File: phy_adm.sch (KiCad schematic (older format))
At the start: 28 parts, among them U7 88E1545, U8 DSC1122CE1-125

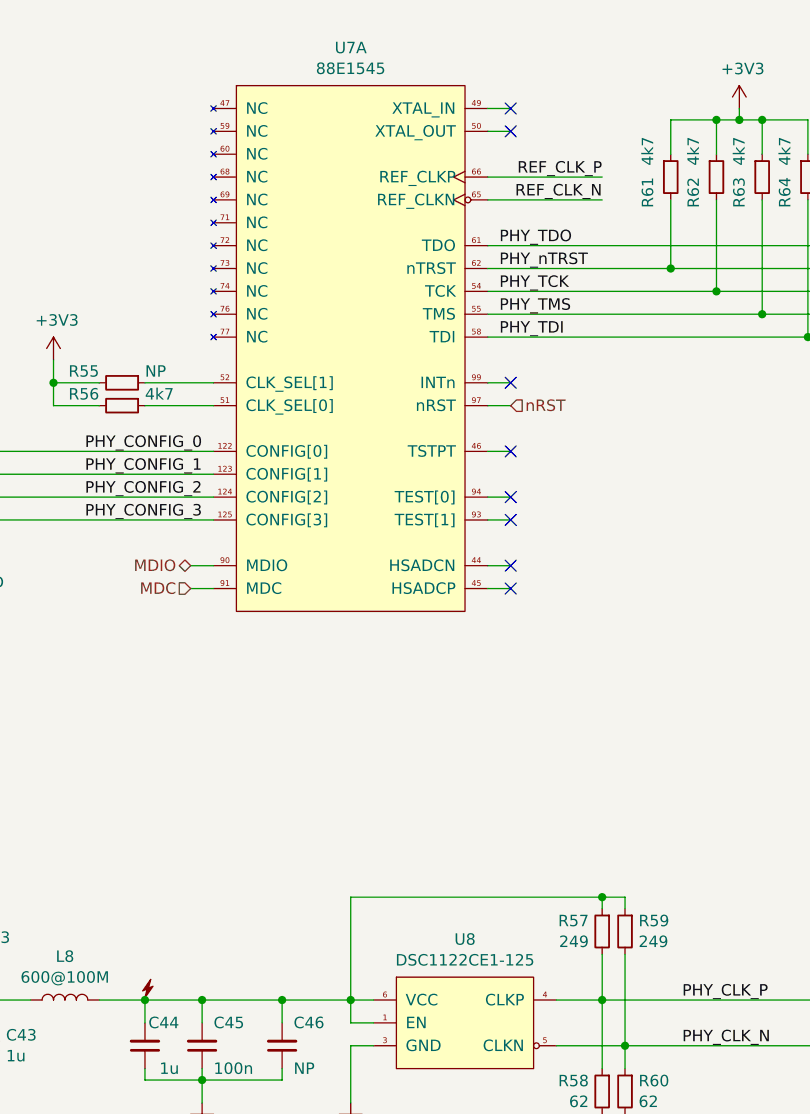
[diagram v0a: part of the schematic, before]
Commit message: lib, sch: Fix connectors refdes letter
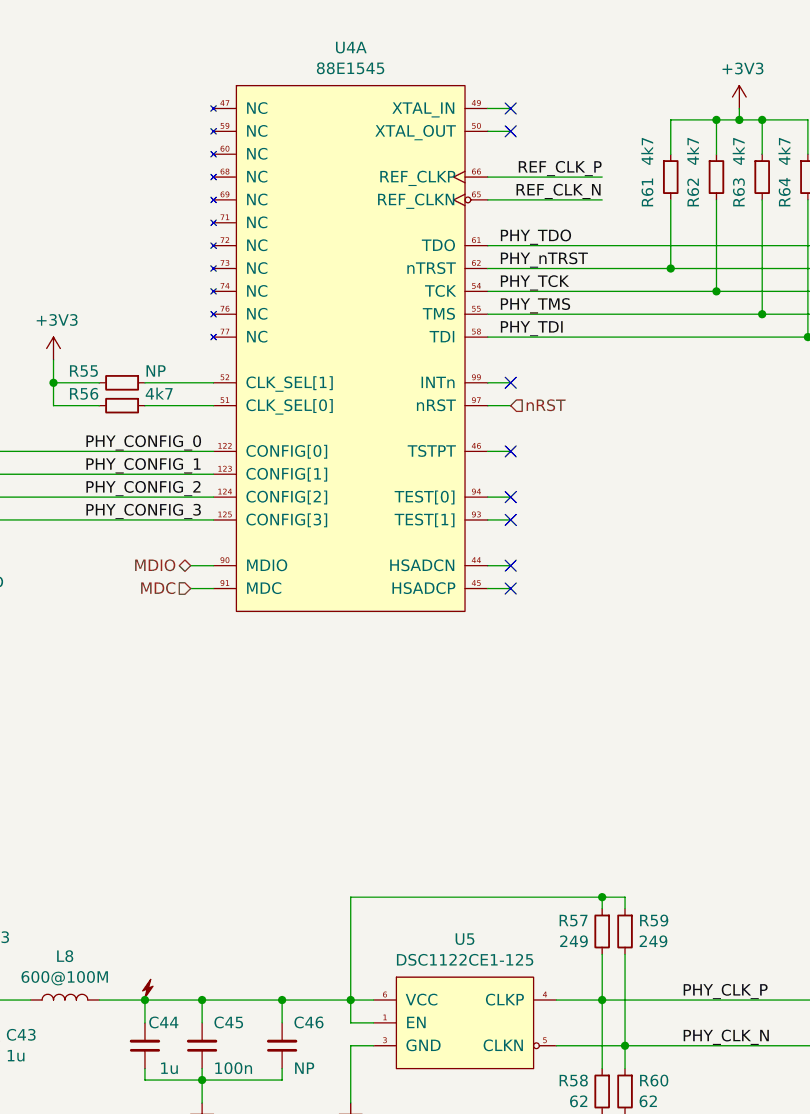
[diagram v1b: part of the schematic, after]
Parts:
- renumbered U7 to U4, U8 to U5
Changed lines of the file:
@@
 $EndDescr
 $Comp
-L pimouss-motherboard:88E1545 U7
+L pimouss-motherboard:88E1545 U4
 U 1 1 5C7D3E15
 P 4000 1300
-F 0 "U7" H 4500 1465 50  0000 C CNN
+F 0 "U4" H 4500 1465 50  0000 C CNN
 F 1 "88E1545" H 4500 1374 50  0000 C CNN
 F 2 "pimouss-motherboard:LQFP-128-1EP_14x20mm_P0.5mm_EP3.93x6.42mm" H 5450 -1100 50  0001 C CNN
@@
 $EndComp
 $Comp
-L pimouss-motherboard:DSC1122CE1-125 U8
+L pimouss-motherboard:DSC1122CE1-125 U5
 U 1 1 5C7D516B
 P 4700 5200
-F 0 "U8" H 5000 5365 50  0000 C CNN
+F 0 "U5" H 5000 5365 50  0000 C CNN
 F 1 "DSC1122CE1-125" H 5000 5274 50  0000 C CNN
 F 2 "pimouss-motherboard:DFN-6_2.5x2mm_P0.825mm" H 5650 4700 50  0001 C CNN

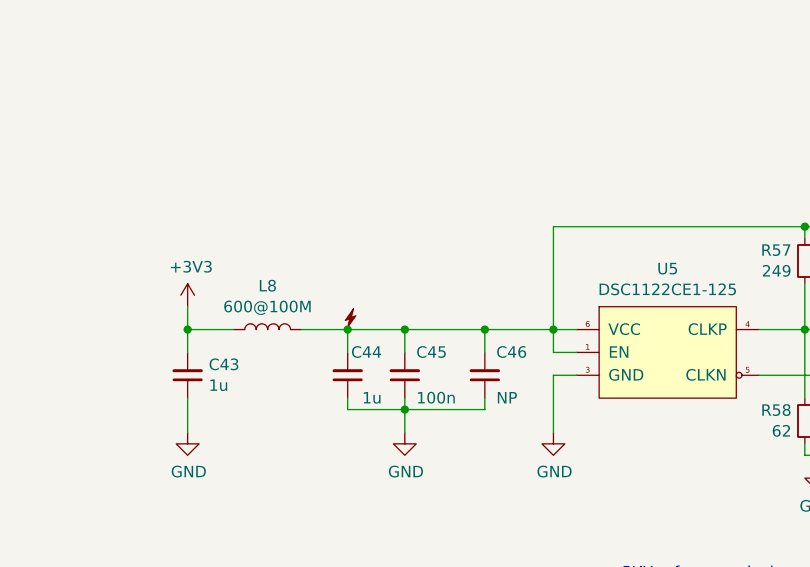
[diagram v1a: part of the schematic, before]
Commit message: sch, pcb: Add testpads on lots of signals
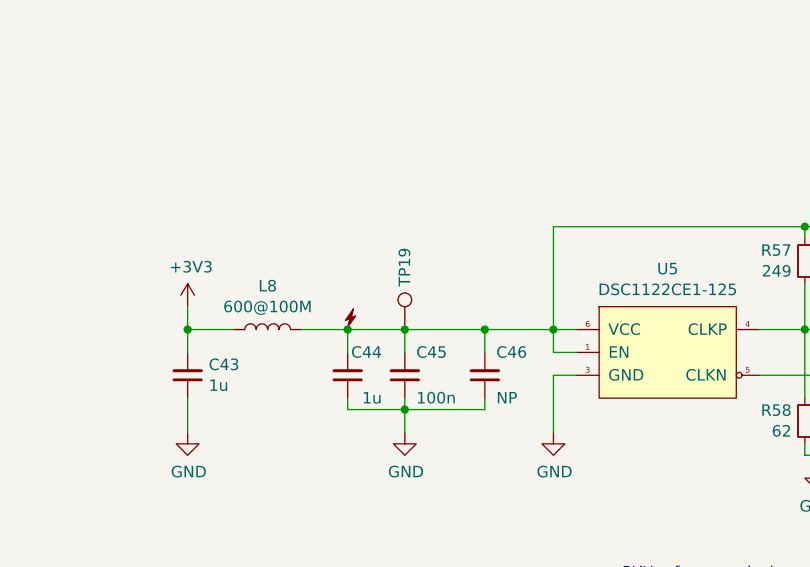
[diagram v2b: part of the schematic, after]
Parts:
- added TP19: TestPoint, TestPoint:TestPoint_Pad_D1.0mm, symbol Connector:TestPoint
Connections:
- net at C44.2, C45.2, C46.2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: now also TP19.1
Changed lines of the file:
@@
+	1    0    0    -1
+$EndComp
+$Comp
+L Connector:TestPoint TP19
+U 1 1 5D405B46
+P 3850 5300
+AR Path="/5D05A5E1/5D405B46" Ref="TP19"  Part="1"
+AR Path="/5CE77C37/5D405B46" Ref="TP?"  Part="1"
+F 0 "TP19" V 3850 5488 50  0000 L CNN
+F 1 "TestPoint" V 3895 5488 50  0001 L CNN
+F 2 "TestPoint:TestPoint_Pad_D1.0mm" H 4050 5300 50  0001 C CNN
+F 3 "~" H 4050 5300 50  0001 C CNN
+	1    3850 5300
 	1    0    0    -1
 $EndComp

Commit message: lib, sch, pcb: Use larger footprint for DCS1122
The 3.2x2.5mm chip is WAY easier to source than the 2.5x2
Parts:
- U5: footprint pimouss-motherboard:DFN-6_2.5x2mm_P0.825mm -> pimouss-motherboard:DFN-6_3.2x2.5mm_P0.825mm
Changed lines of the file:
@@
 F 0 "U5" H 5000 5365 50  0000 C CNN
 F 1 "DSC1122CE1-125" H 5000 5274 50  0000 C CNN
-F 2 "pimouss-motherboard:DFN-6_2.5x2mm_P0.825mm" H 5650 4700 50  0001 C CNN
+F 2 "pimouss-motherboard:DFN-6_3.2x2.5mm_P0.825mm" H 5650 4700 50  0001 C CNN
 F 3 "http://ww1.microchip.com/downloads/en/DeviceDoc/DSC1102%20DSC1122%20Datasheet%20MKQBPD11041002-6.pdf" H 4700 5350 50  0001 C CNN
 	1    4700 5200

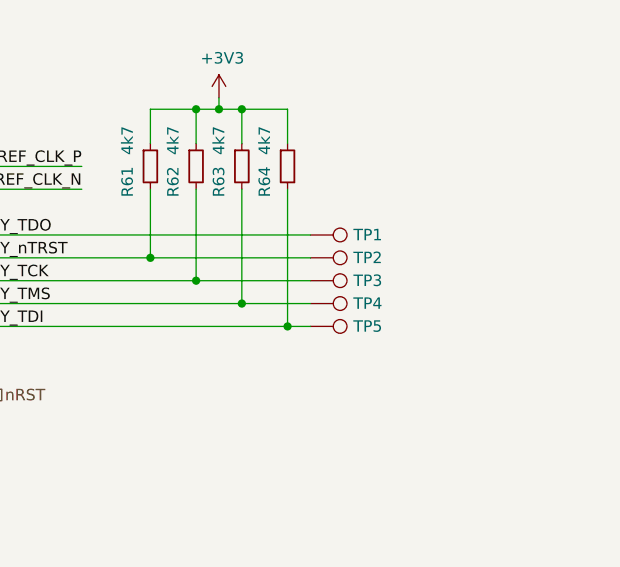
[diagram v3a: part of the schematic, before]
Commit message: sch, pcb: Replace large JTAG headers with 1.27 ones
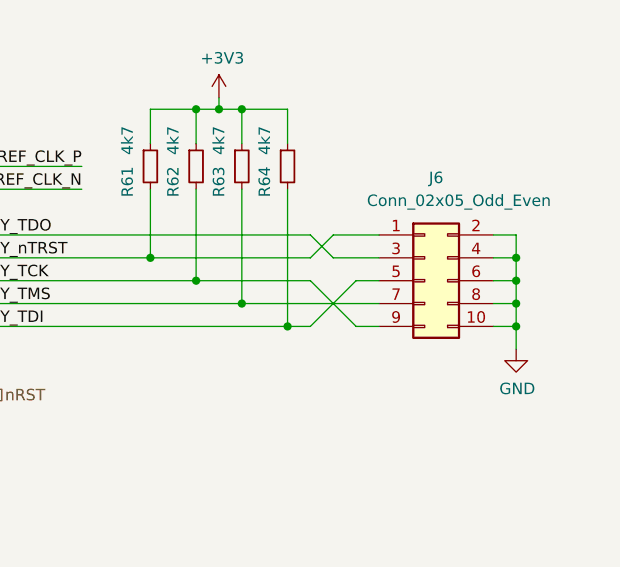
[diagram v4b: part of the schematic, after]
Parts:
- removed TP1, TP2, TP3, TP4, TP5: TestPoint, TestPoint:TestPoint_Pad_D1.0mm, symbol Connector:TestPoint
- added J6: Conn_02x05_Odd_Even, Connector_PinHeader_1.27mm:PinHeader_2x05_P1.27mm_Vertical_SMD, symbol Connector_Generic:Conn_02x05_Odd_Even
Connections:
- net GND: now also J6.10 (Pin_10), J6.2 (Pin_2), J6.4 (Pin_4), J6.6 (Pin_6), J6.8 (Pin_8)
- net PHY_TCK: now also J6.9 (Pin_9)
- net PHY_TDI: now also J6.5 (Pin_5)
- net PHY_TDO: now also J6.3 (Pin_3)
- net PHY_TMS: now also J6.7 (Pin_7)
- net PHY_nTRST: now also J6.1 (Pin_1)
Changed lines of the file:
@@
 	1    0    0    -1
-$EndComp
-$Comp
-L Connector:TestPoint TP5
-U 1 1 5C9A4E5B
-P 6600 2400
-F 0 "TP5" V 6600 2588 50  0000 L CNN
-F 1 "TestPoint" V 6645 2588 50  0001 L CNN
-F 2 "TestPoint:TestPoint_Pad_D1.0mm" H 6800 2400 50  0001 C CNN
-F 3 "~" H 6800 2400 50  0001 C CNN
-	1    6600 2400
-	0    1    1    0
-$EndComp
-$Comp
-L Connector:TestPoint TP4
-U 1 1 5C9A32F5
-P 6600 2300
-F 0 "TP4" V 6600 2488 50  0000 L CNN
-F 1 "TestPoint" V 6645 2488 50  0001 L CNN
-F 2 "TestPoint:TestPoint_Pad_D1.0mm" H 6800 2300 50  0001 C CNN
-F 3 "~" H 6800 2300 50  0001 C CNN
-	1    6600 2300
-	0    1    1    0
-$EndComp
-$Comp
-L Connector:TestPoint TP3
-U 1 1 5C9A1790
-P 6600 2200
-F 0 "TP3" V 6600 2388 50  0000 L CNN
-F 1 "TestPoint" V 6645 2388 50  0001 L CNN
-F 2 "TestPoint:TestPoint_Pad_D1.0mm" H 6800 2200 50  0001 C CNN
-F 3 "~" H 6800 2200 50  0001 C CNN
-	1    6600 2200
-	0    1    1    0
-$EndComp
-$Comp
-L Connector:TestPoint TP2
-U 1 1 5C99FC2A
-P 6600 2100
-F 0 "TP2" V 6600 2288 50  0000 L CNN
-F 1 "TestPoint" V 6645 2288 50  0001 L CNN
-F 2 "TestPoint:TestPoint_Pad_D1.0mm" H 6800 2100 50  0001 C CNN
-F 3 "~" H 6800 2100 50  0001 C CNN
-	1    6600 2100
-	0    1    1    0
-$EndComp
-$Comp
-L Connector:TestPoint TP1
-U 1 1 5C99D9F9
-P 6600 2000
-F 0 "TP1" V 6600 2188 50  0000 L CNN
-F 1 "TestPoint" V 6645 2188 50  0001 L CNN
-F 2 "TestPoint:TestPoint_Pad_D1.0mm" H 6800 2000 50  0001 C CNN
-F 3 "~" H 6800 2000 50  0001 C CNN
-	1    6600 2000
-	0    1    1    0
 $EndComp
 Wire Wire Line
 	5900 2100 6600 2100
-Wire Wire Line
-	5100 2000 6600 2000
 Wire Wire Line
 	5100 2400 6500 2400
@@
 Connection ~ 6100 1450
 Connection ~ 6100 2200
-Wire Wire Line
-	6100 2200 6600 2200
 Connection ~ 6300 1450
 Connection ~ 6300 2300
-Wire Wire Line
-	6300 2300 6600 2300
 Wire Wire Line
 	6300 1450 6500 1450
@@
 	1    0    0    -1
 $EndComp
+$Comp
+L Connector_Generic:Conn_02x05_Odd_Even J6
+U 1 1 5DFD1BC7
+P 7100 2200
+F 0 "J6" H 7150 2650 50  0000 C CNN
+F 1 "Conn_02x05_Odd_Even" H 7250 2550 50  0000 C CNN
+F 2 "Connector_PinHeader_1.27mm:PinHeader_2x05_P1.27mm_Vertical_SMD" H 7100 2200 50  0001 C CNN
+F 3 "~" H 7100 2200 50  0001 C CNN
+	1    7100 2200
+	1    0    0    -1
+$EndComp
+Wire Wire Line
+	7500 2000 7500 2100
+$Comp
+L power:GND #PWR048
+U 1 1 5DFE1CF2
+P 7500 2500
+F 0 "#PWR048" H 7500 2250 50  0001 C CNN
+F 1 "GND" H 7505 2327 50  0000 C CNN
+F 2 "" H 7500 2500 50  0001 C CNN
+F 3 "" H 7500 2500 50  0001 C CNN
+	1    7500 2500
+	1    0    0    -1
+$EndComp
+Wire Wire Line
+	7400 2000 7500 2000
+Wire Wire Line
+	7500 2100 7400 2100
+Wire Wire Line
+	7400 2200 7500 2200
+Wire Wire Line
+	7500 2300 7400 2300
+Wire Wire Line
+	7400 2400 7500 2400
+Connection ~ 7500 2100
+Wire Wire Line
+	7500 2100 7500 2200
+Connection ~ 7500 2200
+Wire Wire Line
+	7500 2200 7500 2300
+Connection ~ 7500 2300
+Wire Wire Line
+	7500 2300 7500 2400
+Connection ~ 7500 2400
+Wire Wire Line
+	7500 2400 7500 2500
+Wire Wire Line
+	6100 2200 6600 2200
+Wire Wire Line
+	5100 2000 6600 2000
+Wire Wire Line
+	6600 2000 6700 2100
+Wire Wire Line
+	6600 2100 6700 2000
+Wire Wire Line
+	6600 2200 6800 2400
+Wire Wire Line
+	6600 2400 6800 2200
+Wire Wire Line
+	6700 2000 6900 2000
+Wire Wire Line
+	6700 2100 6900 2100
+Wire Wire Line
+	6800 2200 6900 2200
+Wire Wire Line
+	6800 2400 6900 2400
+Wire Wire Line
+	6300 2300 6900 2300
 $EndSCHEMATC
